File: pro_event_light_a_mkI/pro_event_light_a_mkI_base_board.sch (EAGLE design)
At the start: 48 parts, among them K1 62201021121, SW1 ALPS_EC11D

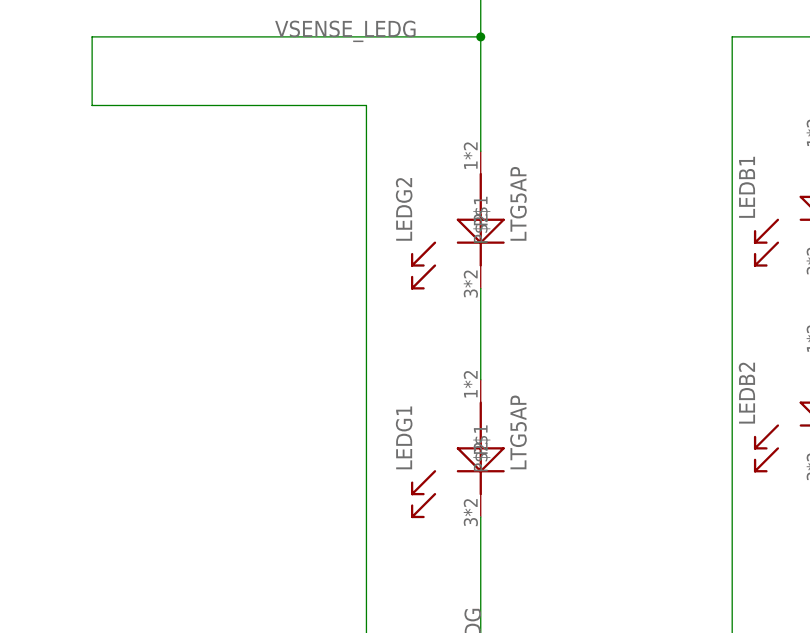
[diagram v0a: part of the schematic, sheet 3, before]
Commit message: first layout for LEDs
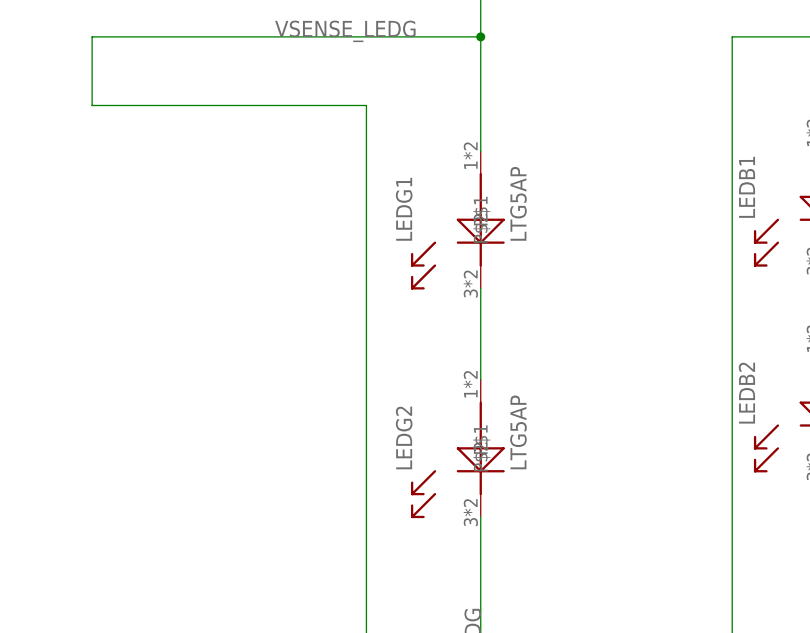
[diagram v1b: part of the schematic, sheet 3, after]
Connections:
- net DRIVER_LEDG: now also LEDG2.P$2; no longer LEDG1.P$2
- net N$3: now also LEDG1.P$2, LEDG2.P$1; no longer LEDG1.P$1, LEDG2.P$2
- net VSENSE_LEDG: now also LEDG1.P$1; no longer LEDG2.P$1
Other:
- moved on the sheet: LEDG1, LEDG2
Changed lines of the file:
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@@
 <part name="LEDB3" library="mod_eagle_library_discrete_elements" deviceset="LDG5AP" device=""/>
 <part name="LEDB4" library="mod_eagle_library_discrete_elements" deviceset="LDG5AP" device=""/>
+<part name="LEDG1" library="mod_eagle_library_discrete_elements" deviceset="LTG5AP" device=""/>
 <part name="LEDG2" library="mod_eagle_library_discrete_elements" deviceset="LTG5AP" device=""/>
-<part name="LEDG1" library="mod_eagle_library_discrete_elements" deviceset="LTG5AP" device=""/>
 <part name="LEDR1" library="mod_eagle_library_discrete_elements" deviceset="LRG5AP" device=""/>
 <part name="LEDR2" library="mod_eagle_library_discrete_elements" deviceset="LRG5AP" device=""/>
@@
 <instance part="LEDB3" gate="G$1" x="172.72" y="193.04"/>
 <instance part="LEDB4" gate="G$1" x="172.72" y="170.18"/>
-<instance part="LEDG2" gate="G$1" x="111.76" y="190.5"/>
-<instance part="LEDG1" gate="G$1" x="111.76" y="165.1"/>
+<instance part="LEDG1" gate="G$1" x="111.76" y="190.5"/>
+<instance part="LEDG2" gate="G$1" x="111.76" y="165.1"/>
 <instance part="LEDR1" gate="G$1" x="226.06" y="187.96"/>
 <instance part="LEDR2" gate="G$1" x="226.06" y="165.1"/>
@@
 <net name="N$3" class="0">
 <segment>
-<pinref part="LEDG2" gate="G$1" pin="P$2"/>
-<pinref part="LEDG1" gate="G$1" pin="P$1"/>
+<pinref part="LEDG1" gate="G$1" pin="P$2"/>
+<pinref part="LEDG2" gate="G$1" pin="P$1"/>
 <wire x1="111.76" y1="182.88" x2="111.76" y2="172.72" width="0.1524" layer="91"/>
 </segment>
@@
 <net name="DRIVER_LEDG" class="0">
 <segment>
-<pinref part="LEDG1" gate="G$1" pin="P$2"/>
+<pinref part="LEDG2" gate="G$1" pin="P$2"/>
 <label x="111.76" y="132.08" size="1.778" layer="95" rot="R90"/>
 <wire x1="111.76" y1="157.48" x2="111.76" y2="104.14" width="0.1524" layer="91"/>
@@
 <net name="VSENSE_LEDG" class="0">
 <segment>
-<pinref part="LEDG2" gate="G$1" pin="P$1"/>
+<pinref part="LEDG1" gate="G$1" pin="P$1"/>
 <wire x1="111.76" y1="215.9" x2="111.76" y2="210.82" width="0.1524" layer="91"/>
 <pinref part="R6" gate="G$1" pin="1"/>

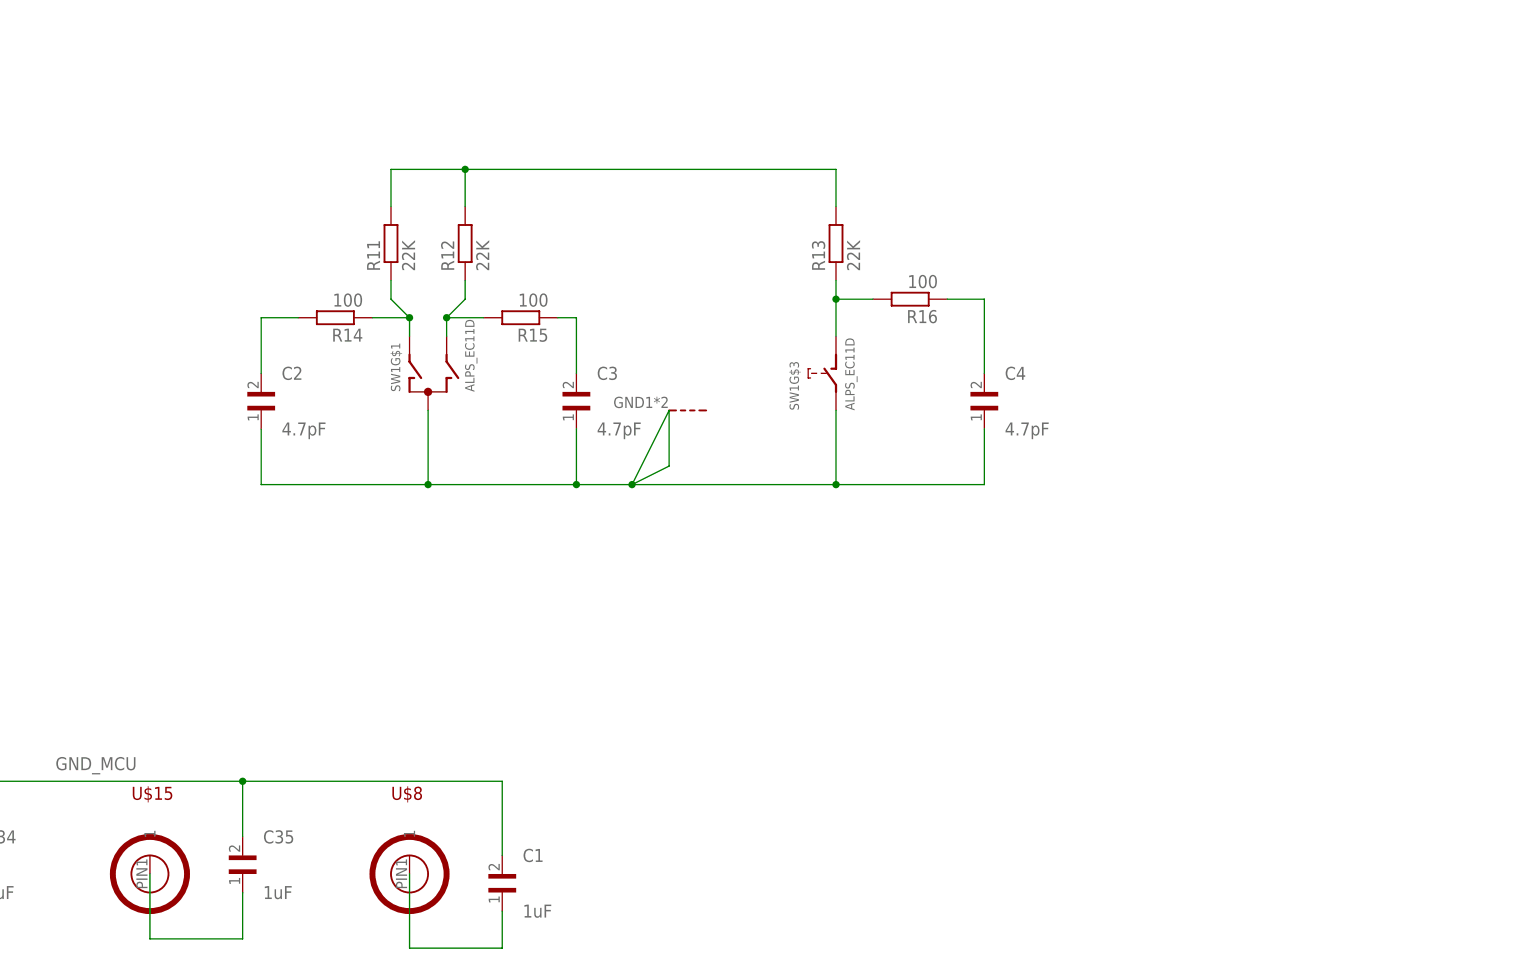
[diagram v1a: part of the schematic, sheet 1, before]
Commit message: cannot accomplished one board, hence split up into two boards
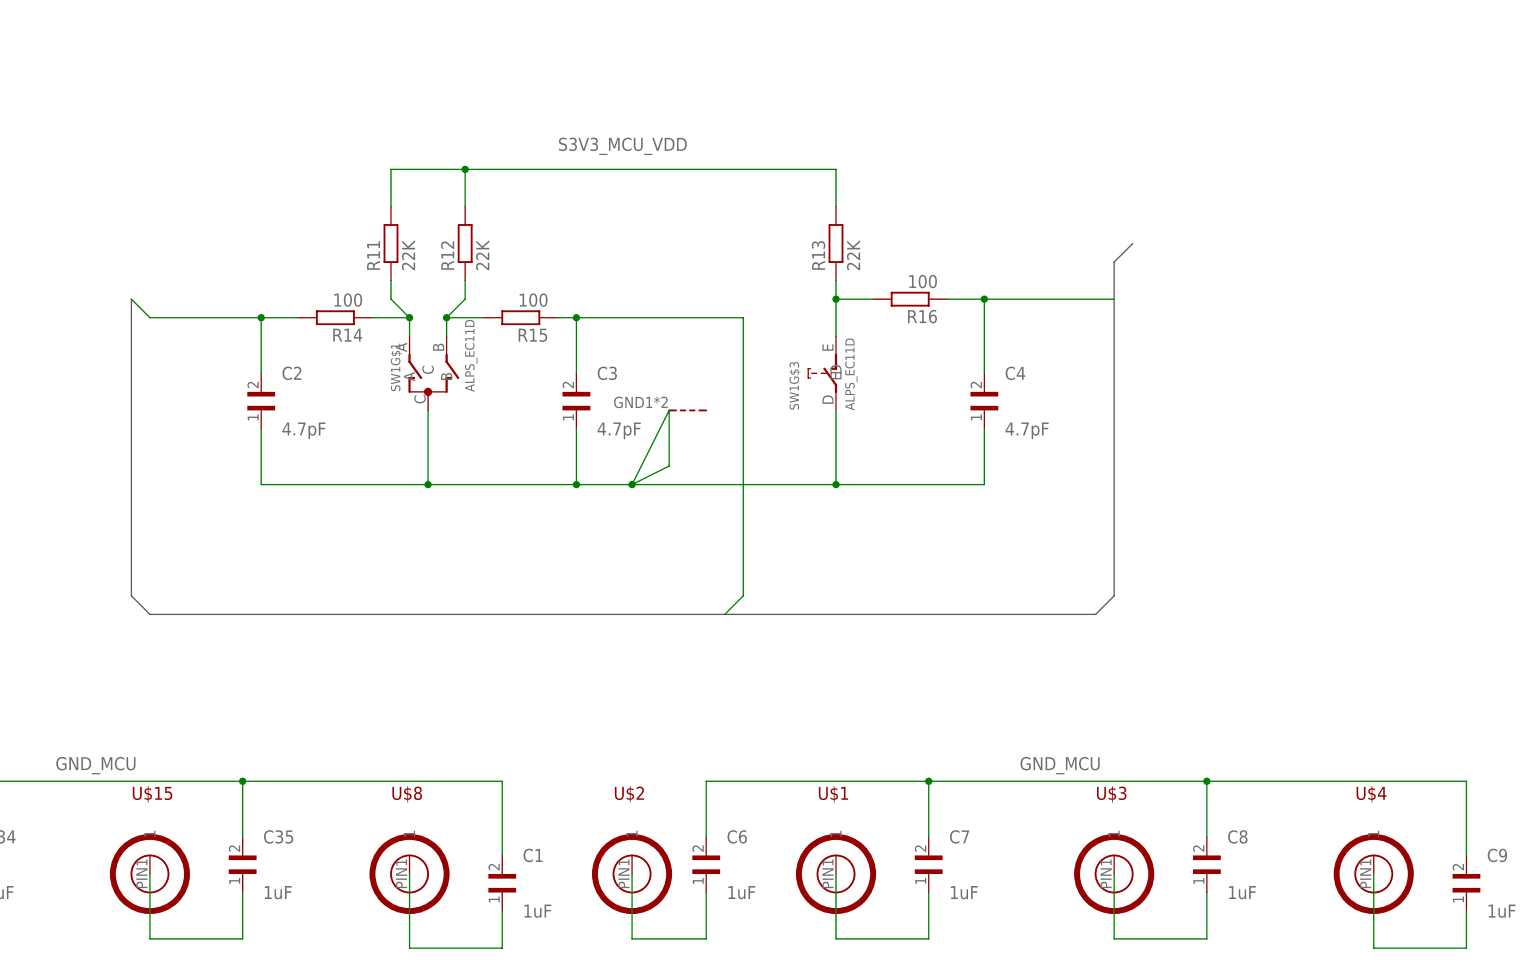
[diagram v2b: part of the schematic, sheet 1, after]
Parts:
- added C6, C7, C8, C9: 1uF, Eagle_Wurth_Elektronik_Passive_Capacitors_rev15a:WCAP-CSGP_1206
- added U$1, U$2, U$3, U$4: (no value), mod-eagle_library_standard_passive_parts:PCB_MOUNTING_HOLES_M3
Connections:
- removed net N$13: C2.2, R14.2
- new net ENCODER_A: C2.2, MCU1G$1.PB0, R14.2
- new net ENCODER_B: C3.2, MCU1G$1.PB1, R15.1
- new net ENCODER_D: C4.2, MCU1G$1.PB2, R16.1
- new net N$28: U$4.COMP, U$4.VC
- new net PMIC_IL4001_S24V: C8.2
- net GND_MCU: now also C2.1, C3.1, C4.1, C6.2, C7.2, C8.2, C9.2, SW1G$1.C, SW1G$2.G, SW1G$3.D
- net LEDB: now also MCU1G$1.PA1; no longer MCU1G$1.PB14
- net LEDG: now also MCU1G$1.PA0; no longer MCU1G$1.PB15
- net LEDR: now also MCU1G$1.PA2; no longer MCU1G$1.PB13
- net LEDW: now also MCU1G$1.PA3; no longer MCU1G$1.PB12
- net N$10: now also C8.1, U$3.1; no longer R11.2, R12.2, R13.2
- net N$11: now also C9.1, U$4.1; no longer C3.2, R15.1
- net N$30: now also C7.1, U$4.SHDN
- net N$35: now also U$4.FB
- net N$5: now also C6.1, U$2.1; no longer C2.1, C3.1, C4.1, SW1G$1.C, SW1G$2.G, SW1G$3.D
- net N$8: now also C7.1, U$1.1; no longer C4.2, R16.1
- net PMIC_IL4001_GND: now also C8.1
- net PMIC_LT1936_BOOST: now also U$4.BOOST
- net PMIC_LT1936_GND: now also C6.2, C7.2, U$4.GND1, U$4.GND2
- net PMIC_LT1936_SW: now also U$4.SW
- net PMIC_LT1936_VIN: now also C6.1, U$4.VIN
- net S3V3_MCU_VDD: now also R11.2, R12.2, R13.2
